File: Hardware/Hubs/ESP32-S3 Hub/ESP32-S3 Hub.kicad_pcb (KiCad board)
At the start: 6 copper layers, 15 x 30 mm, 59 parts, among them J1 Precidip 853-87-004-20-001101, J10 Precidip 853-87-004-20-001101, J11 7 pin FPC 0.3mm Aces 51688-00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, J12 Precidip 853-87-004-20-001101, J13 TE 3-2363961-0 receptacle, J15 Precidip 853-87-004-20-001101, J16 TE 3-2363961-0 receptacle, J18 Precidip 852-10-004-20-001101, J2 Precidip 853-87-004-20-001101, J3 7 pin FPC 0.3mm Aces 51688-00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, J4 Precidip 853-87-004-20-001101, J5 7 pin FPC 0.3mm Aces 51688-00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, J6 Precidip 853-87-004-20-001101, J7 Precidip 853-87-004-20-001101, J8 7 pin FPC 0.3mm Aces 51688-00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, J9 Precidip 853-87-004-20-001101, SW1 Mitsumi R-667996, SW2 Mitsumi R-667996, U1 ESP32-S3, U2 74HC595, U3 THVD1420DRLR, Y1 ABM11-40.000MHZ-B1U-T3, 10ppm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

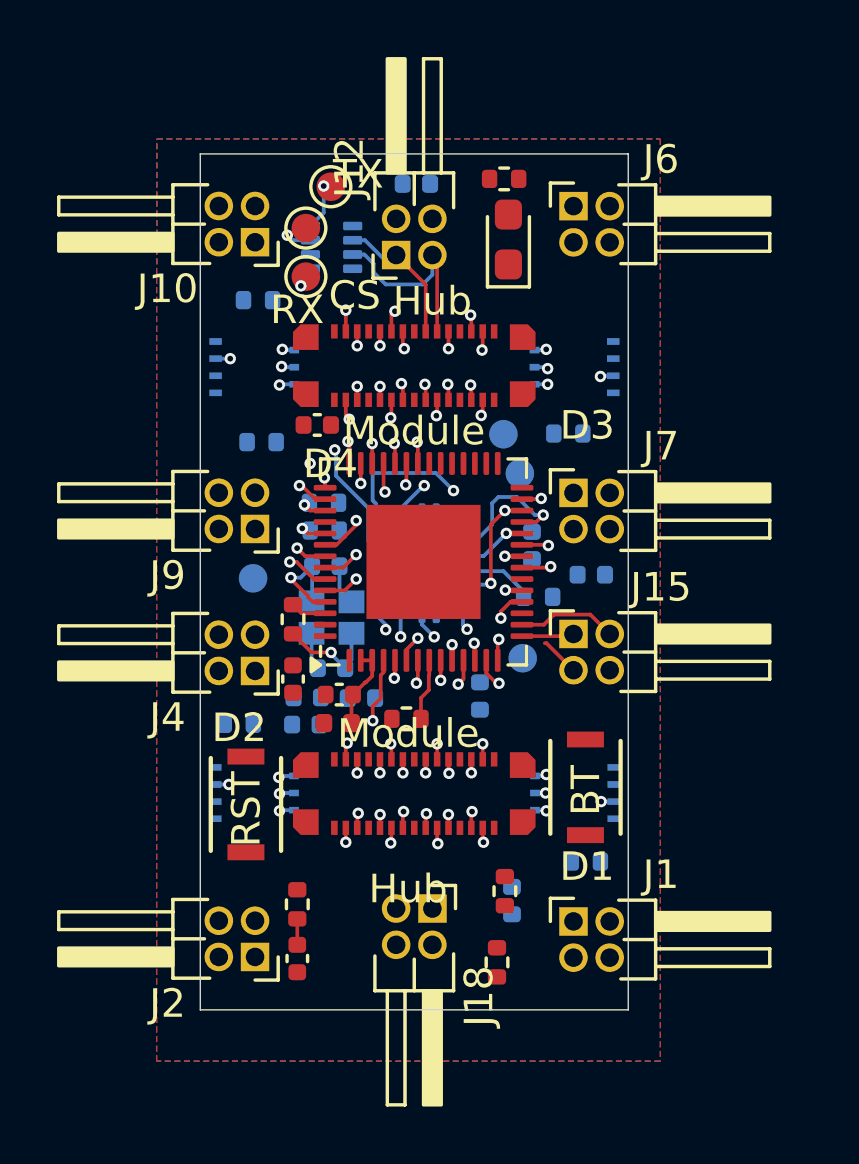
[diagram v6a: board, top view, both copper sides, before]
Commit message: Swapped out footprints on pcb, started routing
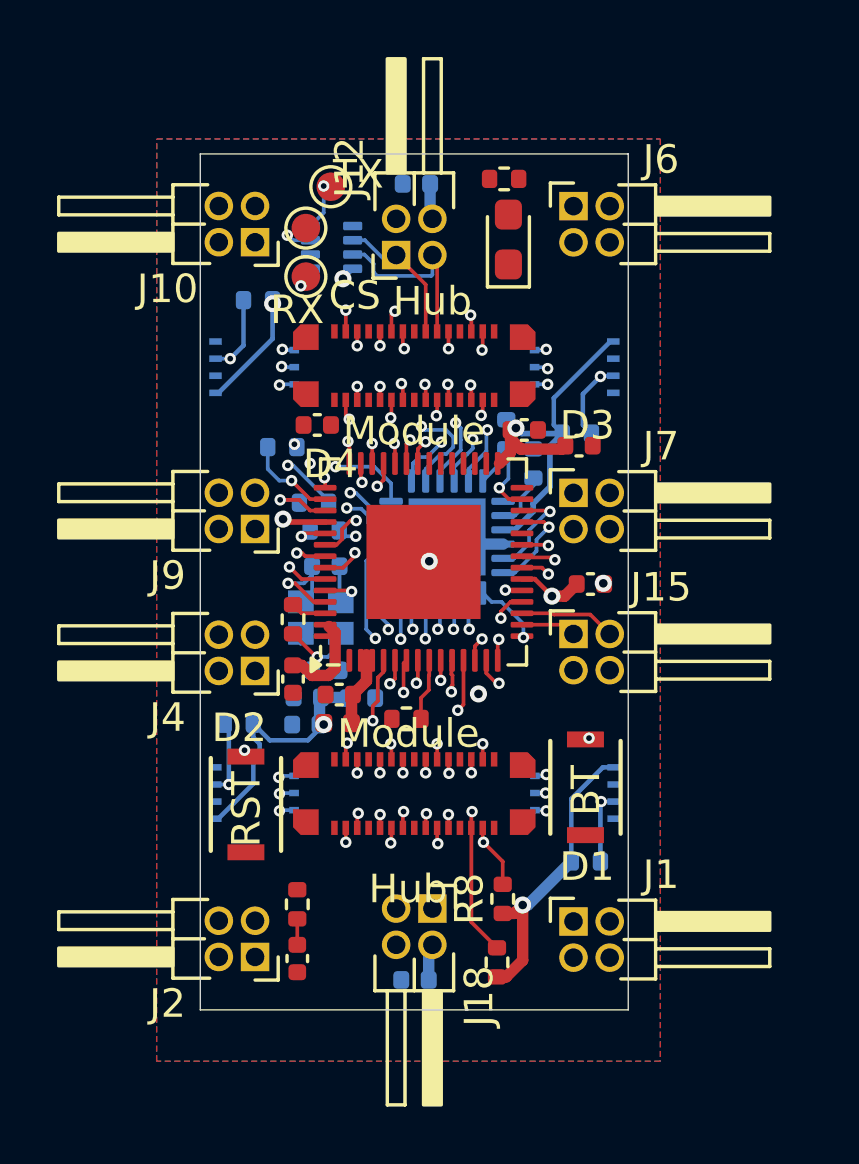
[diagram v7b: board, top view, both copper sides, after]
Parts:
- removed TP1: S-EN, TestPoint:TestPoint_Pad_D1.0mm
- removed TP12: SRCLK, TestPoint:TestPoint_Pad_D1.0mm
- removed TP14: SER, TestPoint:TestPoint_Pad_D1.0mm
- removed TP4: IO46, TestPoint:TestPoint_Pad_D1.0mm
- added R12: 1.8k, Resistor_SMD:R_0402_1005Metric, B.Cu at (159.6, 92.7)
- C5, C7, C8: moved to F.Cu
- U2: value 74HC595 -> IS31FL3726A-QFLS4; footprint Package_DFN_QFN:DHVQFN-16-1EP_2.5x3.5mm_P0.5mm_EP1x2mm -> Package_DFN_QFN:QFN-24-1EP_4x4mm_P0.5mm_EP2.7x2.7mm
- moved R11 5.81 mm to (158.6, 91.6), turned to 90 degrees
- moved C5 5.59 mm to (159.3, 91.5)
- moved C8 5.52 mm to (161.6, 96.9), turned to 0 degrees
- moved C14 4.39 mm to (155.4, 110.8), turned to 180 degrees
- moved C7 3.87 mm to (161.2, 92.0), turned to 0 degrees
- moved U2 1.12 mm to (156.6, 95.2), turned to 180 degrees
- moved R3 0.75 mm to (150.8, 92.1)
- moved Y1 0.38 mm to (152.1, 98.0)
- moved R4 0.35 mm to (151.9, 94.0)
- moved R19 0.30 mm to (161.1, 91.6)
- moved R8 0.28 mm to (158.5, 107.9)
- moved C11 0.21 mm to (152.3, 99.9), turned to 0 degrees
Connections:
- J13 pad 11: RS485+ -> UART0_TX
- J13 pad 13: RS485- -> UART0_RX
- J13 pad 18: RS485- -> UART0_RX
- J13 pad 20: RS485+ -> UART0_TX
- J13 pad 22: Free1 -> NRST
- J13 pad 26: CS6 -> Free1
- J13 pad 28: CS5 -> unconnected-(J13-Pin_28-Pad28)
- J13 pad 3: CS5 -> unconnected-(J13-Pin_3-Pad3)
- J13 pad 5: CS6 -> Free1
- J13 pad 9: Free1 -> NRST
- J16 pad 11: RS485+ -> UART0_TX
- J16 pad 13: RS485- -> UART0_RX
- J16 pad 18: RS485- -> UART0_RX
- J16 pad 20: RS485+ -> UART0_TX
- J16 pad 22: Free2 -> NRST
- J16 pad 26: CS8 -> Free2
- J16 pad 28: CS7 -> unconnected-(J16-Pin_28-Pad28)
- J16 pad 3: CS7 -> unconnected-(J16-Pin_3-Pad3)
- J16 pad 5: CS8 -> Free2
- J16 pad 9: Free2 -> NRST
- U1 pad 10: 3CSA-A -> 4CSA-D
- U1 pad 11: 2CSA-A -> 3CSA-B
- U1 pad 12: 2CSA-B -> 3CSA-A
- U1 pad 13: 1CSA-A -> 3CSA-C
- U1 pad 14: 1CSA-B -> 3CSA-D
- U1 pad 15: 1A -> ShiftLatch
- U1 pad 16: 1B -> 2CSA-A
- U1 pad 17: 1C -> 2CSA-B
- U1 pad 18: 2A -> 2CSA-C
- U1 pad 19: 2B -> 2CSA-D
- U1 pad 21: 2C -> 1CSA-C
- U1 pad 22: 3A -> 1CSA-D
- U1 pad 23: 3B -> 1CSA-A
- U1 pad 24: ShiftRegCLK -> 1CSA-B
- U1 pad 36: 3C -> CS4
- U1 pad 37: 4C -> CS3
- U1 pad 38: 4A -> CS2
- U1 pad 39: 4B -> CS1
- U1 pad 52: Net-(U1-GPIO46) -> GND
- U1 pad 9: 3CSA-B -> 4CSA-C
- U2 pad 1: CS2 -> unconnected-(U2-SERIAL-OUT-Pad1)
- U2 pad 10: unconnected-(U2-~{SRCLR}-Pad10) -> 1B
- U2 pad 11: ShiftCLK -> 1D
- U2 pad 12: ShiftRegCLK -> 2A
- U2 pad 13: ShiftEn -> 2B
- U2 pad 14: ShiftData -> 2C
- U2 pad 15: CS1 -> 2D
- U2 pad 16: VDD -> 3A
- U2 pad 17: GND -> 3B
- U2 pad 2: CS3 -> Net-(U2-R_EXT)
- U2 pad 3: CS4 -> VDD
- U2 pad 4: CS5 -> GND
- U2 pad 5: CS6 -> ShiftData
- U2 pad 6: CS7 -> ShiftCLK
- U2 pad 7: CS8 -> ShiftLatch
- U2 pad 8: GND -> 1C
- U2 pad 9: unconnected-(U2-QH&apos;-Pad9) -> 1A
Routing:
- net VDD: track 0.00 -> 49.0 mm, vias 0 -> 8
- net CS7: track 7.45 -> 0.00 mm, vias 3 -> 0
- net CS6: track 5.84 -> 0.00 mm, vias 3 -> 0
- net SCL1: track 2.46 -> 7.03 mm
- net 2D: track 0.00 -> 3.96 mm, vias 0 -> 1
- net CS8: track 2.96 -> 0.00 mm, vias 3 -> 0
- net 4A: track 0.71 -> 3.32 mm
- net ShiftLatch: track 0.00 -> 2.42 mm, vias 0 -> 1
- net ShiftRegCLK: track 2.40 -> 0.00 mm, vias 1 -> 0
- net NRST: track 3.18 -> 5.46 mm, vias 1 -> 6
- net 2C: track 1.02 -> 3.20 mm
- net GND: track 2.74 -> 4.90 mm, vias 0 -> 3
- net Net-(U1-MTCK): track 1.10 -> 3.22 mm
- net Net-(U2-R_EXT): track 0.00 -> 2.08 mm
- net 4D: track 0.00 -> 2.07 mm, vias 0 -> 1
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
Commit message: Added future design expansion comments, re arrange components to fit better
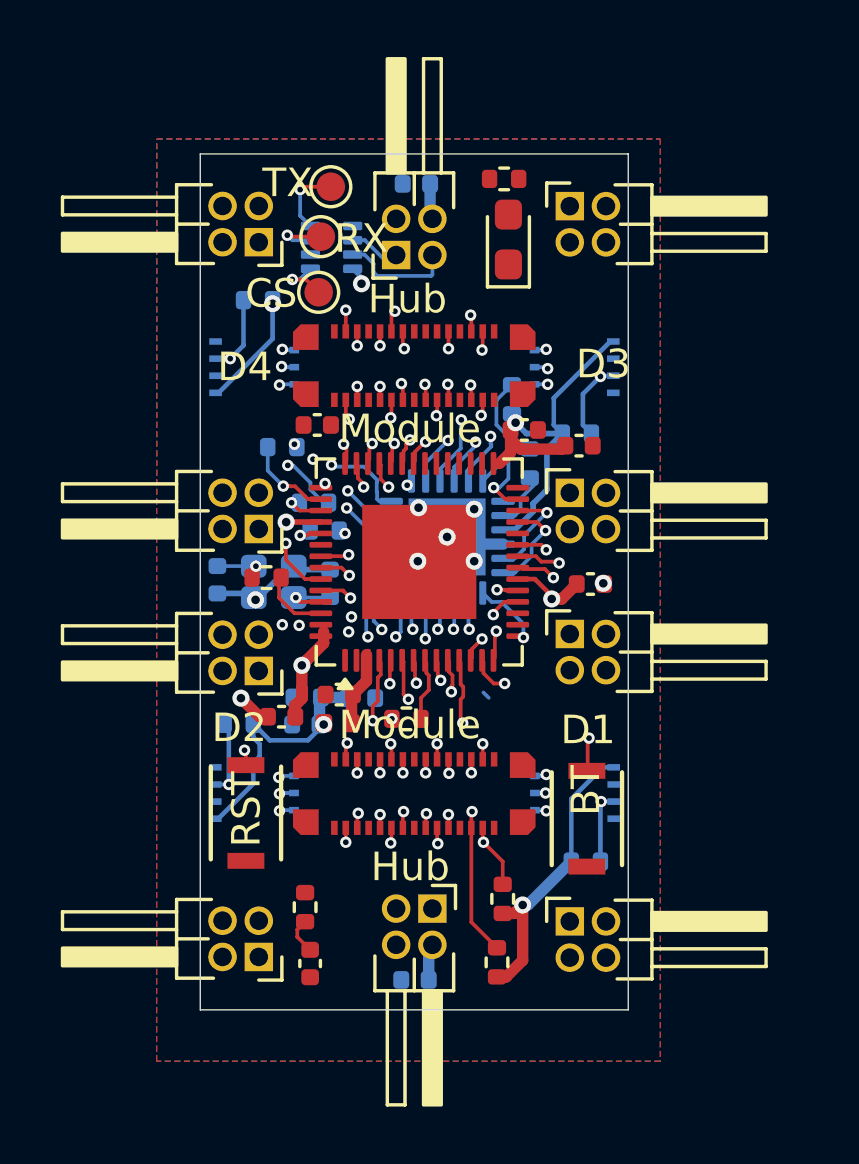
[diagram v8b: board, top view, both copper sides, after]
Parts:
- moved C11 4.95 mm to (148.5, 96.7), turned to -90 degrees
- moved Y1 2.07 mm to (150.5, 96.8), turned to 180 degrees
- moved R6 1.73 mm to (150.2, 96.7), turned to 0 degrees
- moved C9 1.38 mm to (150.8, 101.5), turned to 0 degrees
- moved R11 1.24 mm to (158.8, 90.4), turned to -90 degrees
- moved SW1 1.10 mm to (161.4, 105.1)
- moved TP2 0.71 mm to (152.1, 86.7)
- moved C12 0.62 mm to (152.4, 96.8), turned to 90 degrees
- moved TP20 0.60 mm to (152.1, 84.7)
- moved C13 0.48 mm to (151.8, 110.2)
- moved SW2 0.30 mm to (149.5, 104.9)
- moved R7 0.29 mm to (151.6, 108.2)
- moved U1 0.15 mm to (155.6, 96.1)
- moved J1 0.13 mm to (160.8, 108.7)
- moved J10 0.13 mm to (149.9, 84.9)
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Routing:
- net GND: track 4.90 -> 9.60 mm, vias 3 -> 14
- net 1B: track 4.68 -> 1.30 mm
- net RS485-: track 5.08 -> 1.98 mm
- net RS485+: track 6.73 -> 3.99 mm
- net ShiftEn: track 4.00 -> 6.61 mm
- net Net-(U1-XTAL_N): track 4.48 -> 2.30 mm
- net 1A: track 3.33 -> 1.28 mm
- net 3D: track 1.96 -> 0.00 mm
- net 4A: track 3.32 -> 1.74 mm
- net Net-(U1-MTDO): track 2.45 -> 1.14 mm
- net Net-(U1-XTAL_P): track 1.25 -> 2.43 mm
- net VDD: track 49.0 -> 50.2 mm
- net BOOT: track 1.04 -> 2.01 mm
- net UART0_RX: track 3.71 -> 4.66 mm
- net UART0_TX: track 4.36 -> 5.26 mm
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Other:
- board text removed: "D+"
- board text removed: "D-"
- board text removed: "IO46"
- board text removed: "SEN"
